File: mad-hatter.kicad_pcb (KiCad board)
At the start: 2 copper layers, 337.2 x 122.6 mm, 161 parts, among them J1 USB_B_Mini, J2 AVR-ISP-6, U1 ATMEGA32U4, X1 16MHz

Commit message: Inverts ISP connector; small fixes
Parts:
- J2: moved to F.Cu
- moved J2 7.85 mm to (304.3, 253.7)
- moved P? 5.39 mm to (305.8, 246.7)
- moved P? 5.39 mm to (310.9, 246.7)
- moved P? 5.39 mm to (308.4, 246.7)
- moved P? 5.39 mm to (303.3, 246.7)
- moved P? 5.39 mm to (298.2, 246.7)
- moved P? 5.39 mm to (300.7, 246.7)
- moved D_PGDN1 4.77 mm to (133.5, 202.7), turned to 180 degrees
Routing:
- net SCK: track 86.4 -> 64.8 mm
- net Net-(D_PGDN1-Pad2): track 5.32 -> 11.3 mm
- net ROW3: track 392.0 -> 387.2 mm
- net +5V: track 164.2 -> 160.0 mm
- net ROW4: track 352.1 -> 354.7 mm
- net MISO: track 55.7 -> 57.7 mm
- net GND: track 107.0 -> 108.0 mm, vias 2 -> 1

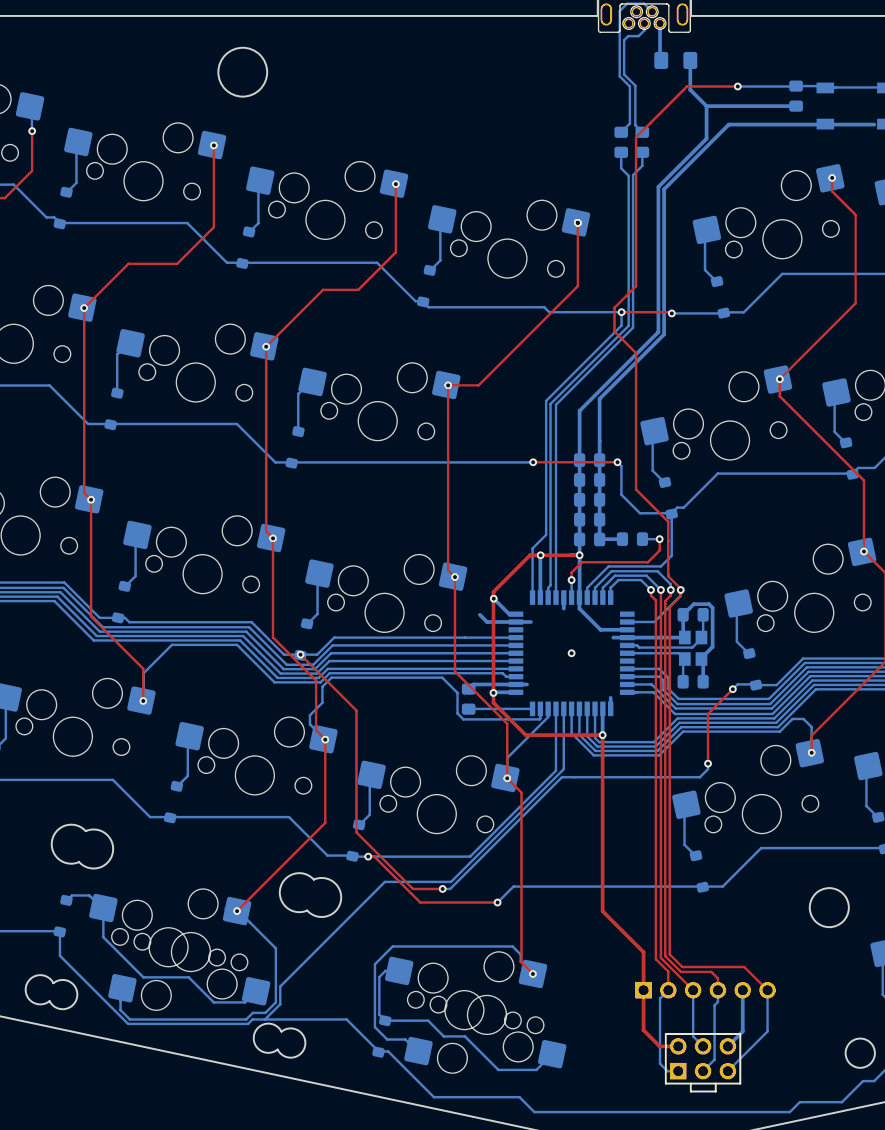
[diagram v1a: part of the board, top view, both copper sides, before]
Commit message: Improves placement of crystal
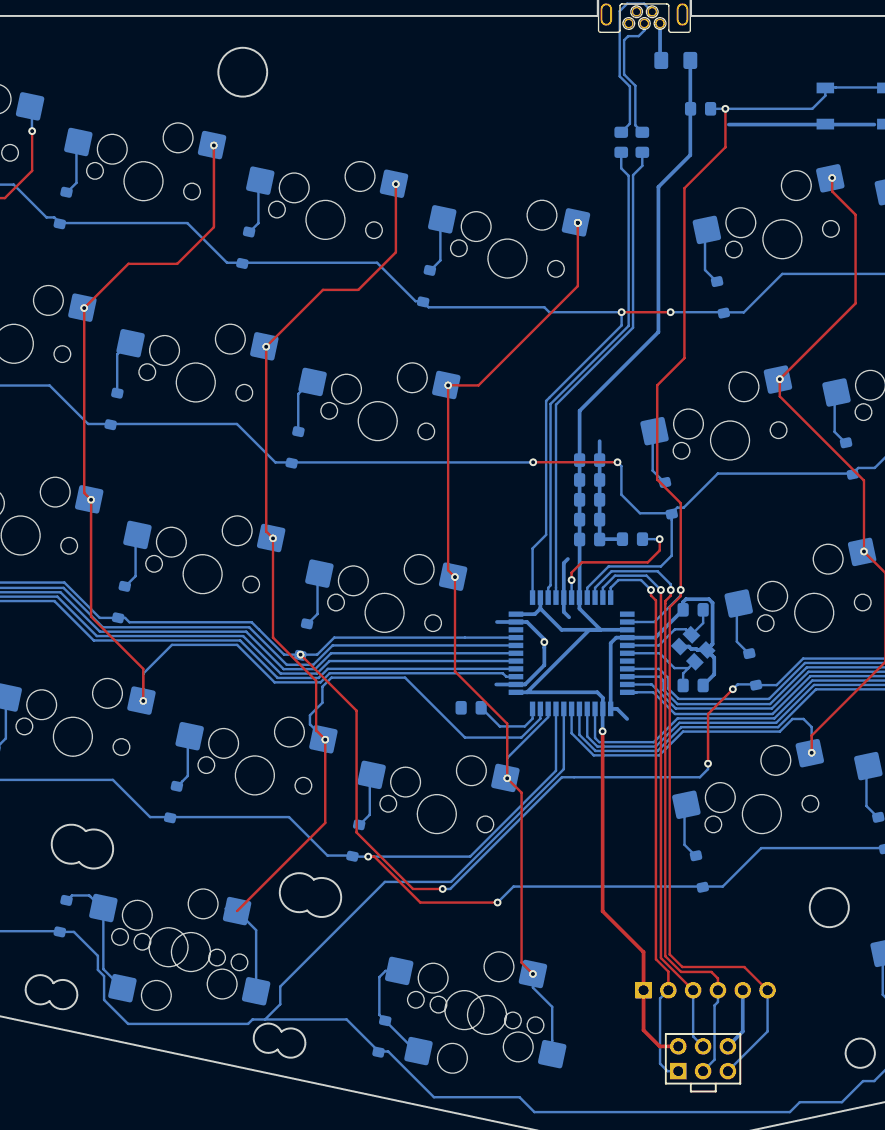
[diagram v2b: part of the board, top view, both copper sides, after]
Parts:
- moved R1 9.87 mm to (304.0, 156.5), turned to 180 degrees
- moved R4 0.92 mm to (280.5, 217.8), turned to 0 degrees
- moved C1 0.51 mm to (303.3, 207.8)
- moved C2 0.38 mm to (303.3, 215.5)
- turned X1 to 315 degrees
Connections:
- J1 pad 6: (no net) -> Net-(J1-Pad6)
- K_GUI1_2 pad 1: COL6 -> Net-(D_GUI1-Pad2)
- K_GUI1_2 pad 2: Net-(D_GUI1-Pad2) -> COL6
- K_SPC1_2 pad 1: COL5 -> Net-(D_SPC1-Pad2)
- K_SPC1_2 pad 2: Net-(D_SPC1-Pad2) -> COL5
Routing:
- net +5V: track 160.0 -> 136.5 mm, vias 5 -> 1
- net COL6: track 127.3 -> 106.1 mm
- net COL5: track 153.3 -> 132.5 mm, vias 5 -> 4
- net GND: track 108.0 -> 88.2 mm
- net Net-(D_GUI1-Pad2): track 26.9 -> 11.7 mm
- net Net-(D_SPC1-Pad2): track 26.2 -> 13.4 mm
- net RST: track 144.4 -> 139.2 mm
- net Net-(C2-Pad1): track 8.54 -> 9.83 mm
- net Net-(R4-Pad2): track 6.55 -> 7.38 mm
- net ROW4: track 354.7 -> 355.5 mm

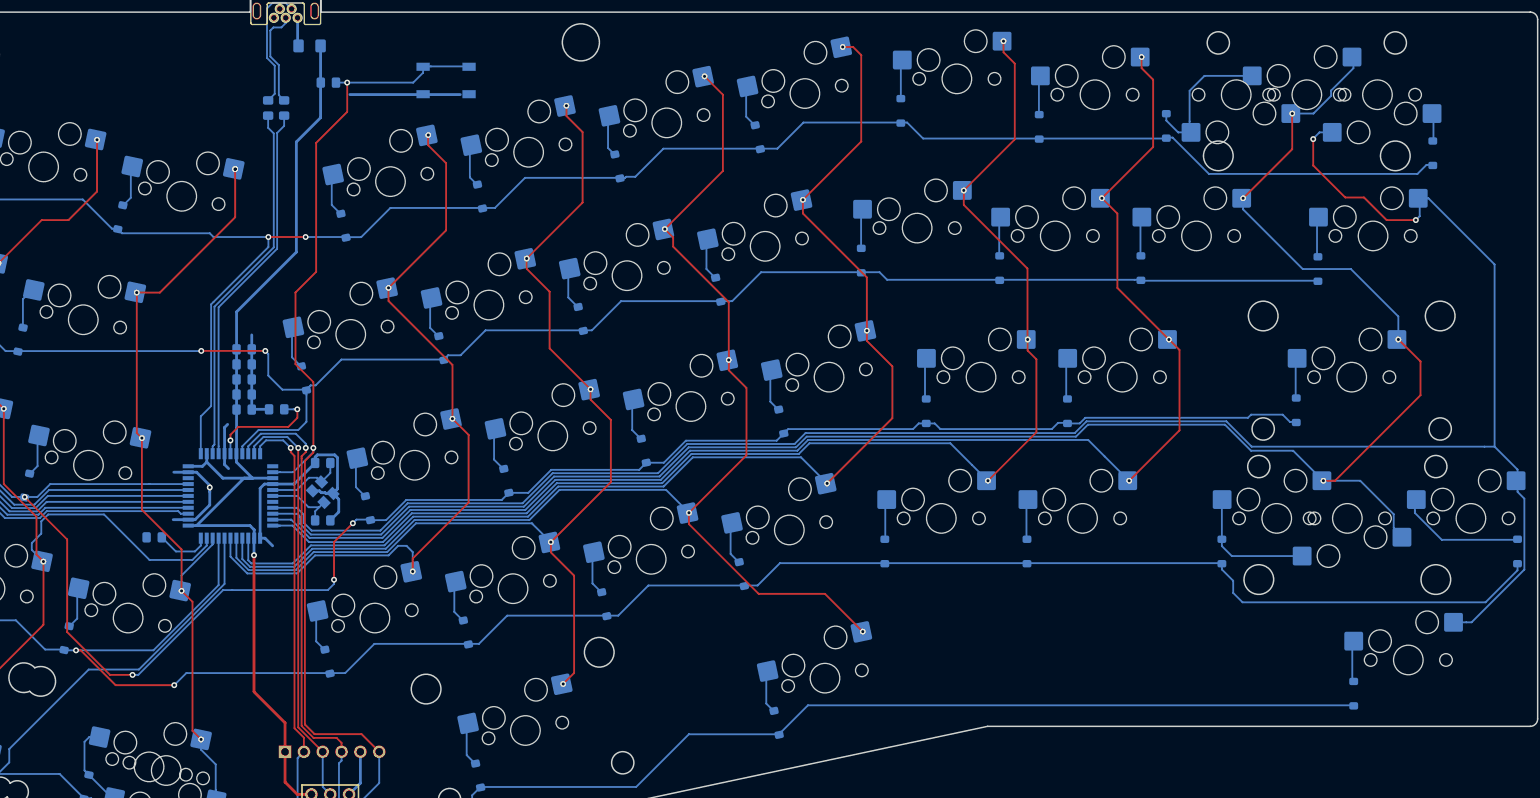
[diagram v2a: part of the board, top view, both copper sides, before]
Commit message: Reorganize capacitors
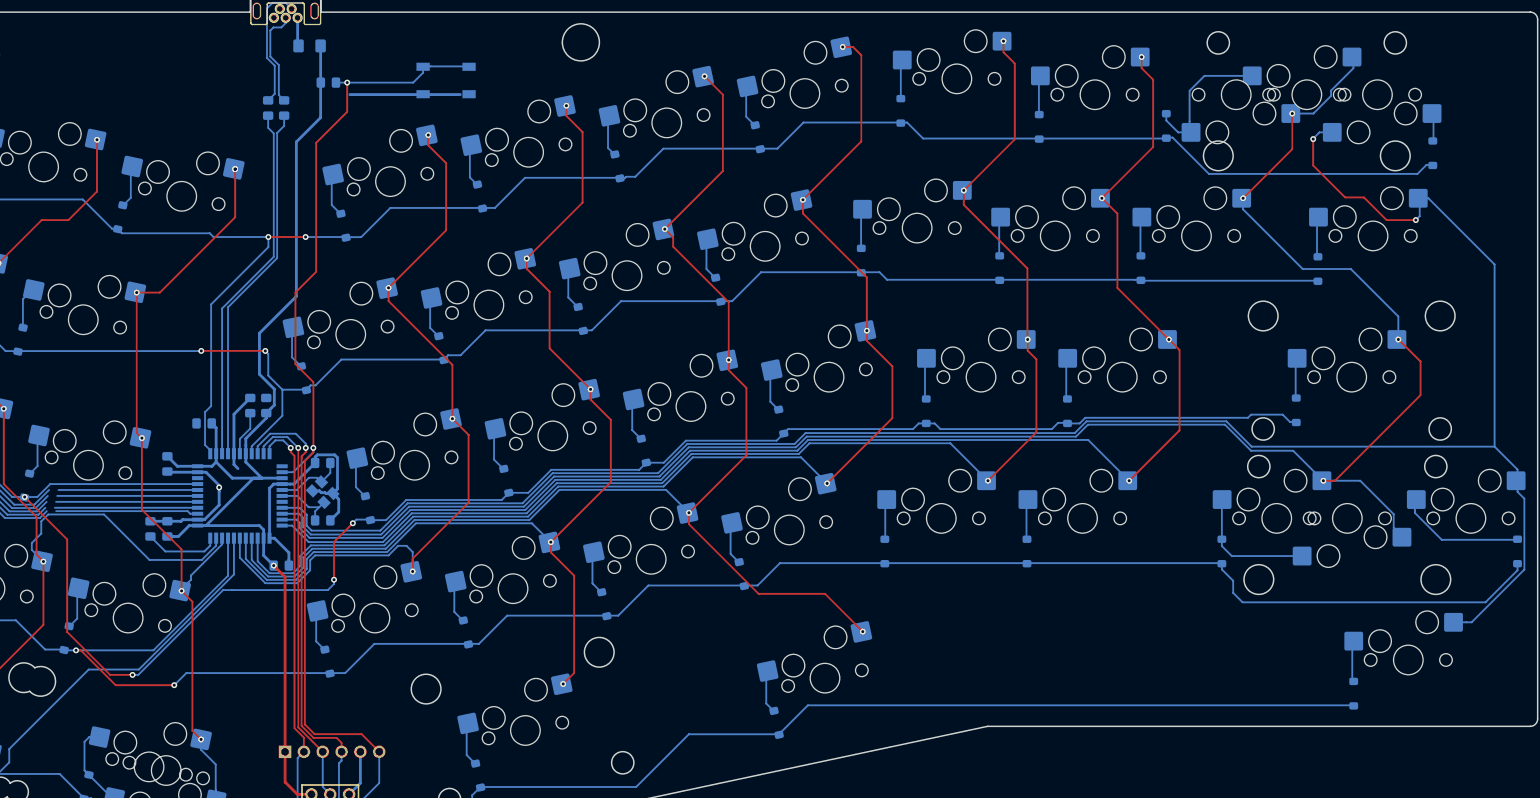
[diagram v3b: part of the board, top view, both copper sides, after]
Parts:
- moved C7 26.3 mm to (282.3, 216.7), turned to 90 degrees
- moved C5 25.6 mm to (297.7, 221.6)
- moved C3 12.7 mm to (282.3, 207.9), turned to 270 degrees
- moved C4 6.66 mm to (287.3, 202.4), turned to 180 degrees
- moved C6 6.30 mm to (295.7, 200.0), turned to 90 degrees
- moved C8 3.60 mm to (293.5, 200.0), turned to 90 degrees
- moved U1 1.27 mm to (292.1, 212.2)
- moved R4 1.25 mm to (280.0, 216.7), turned to 270 degrees
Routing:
- net +5V: track 136.5 -> 151.2 mm
- net Net-(C8-Pad1): track 15.6 -> 6.05 mm, vias 2 -> 0
- net ROW1: track 343.1 -> 338.2 mm
- net Net-(R4-Pad2): track 7.38 -> 10.2 mm
- net COL11: track 175.5 -> 173.3 mm
- net RST: track 139.2 -> 138.0 mm
- net ROW2: track 379.1 -> 380.3 mm
- net Net-(C2-Pad1): track 9.83 -> 8.56 mm
- net Net-(C1-Pad1): track 10.5 -> 9.27 mm
- net MOSI: track 56.6 -> 55.3 mm
- net MISO: track 57.7 -> 56.4 mm
- net SCK: track 64.8 -> 63.5 mm
- net COL5: track 132.5 -> 133.7 mm
- net COL13: track 252.8 -> 251.7 mm
- net COL14: track 269.8 -> 268.7 mm
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
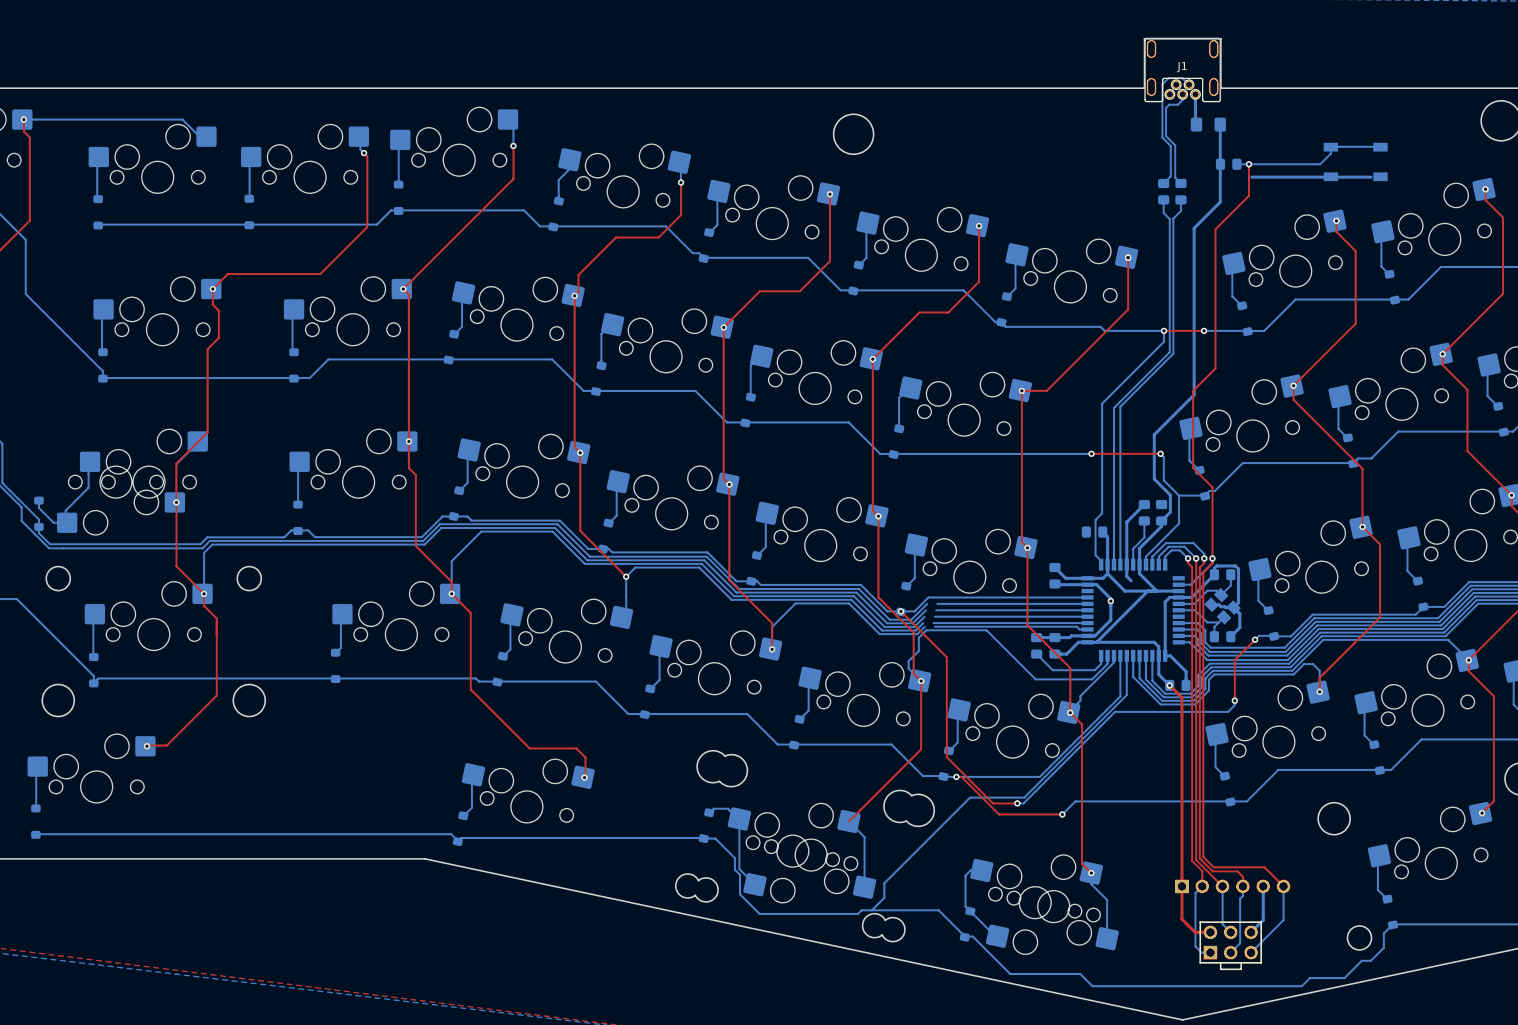
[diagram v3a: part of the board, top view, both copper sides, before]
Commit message: Improves caps placement
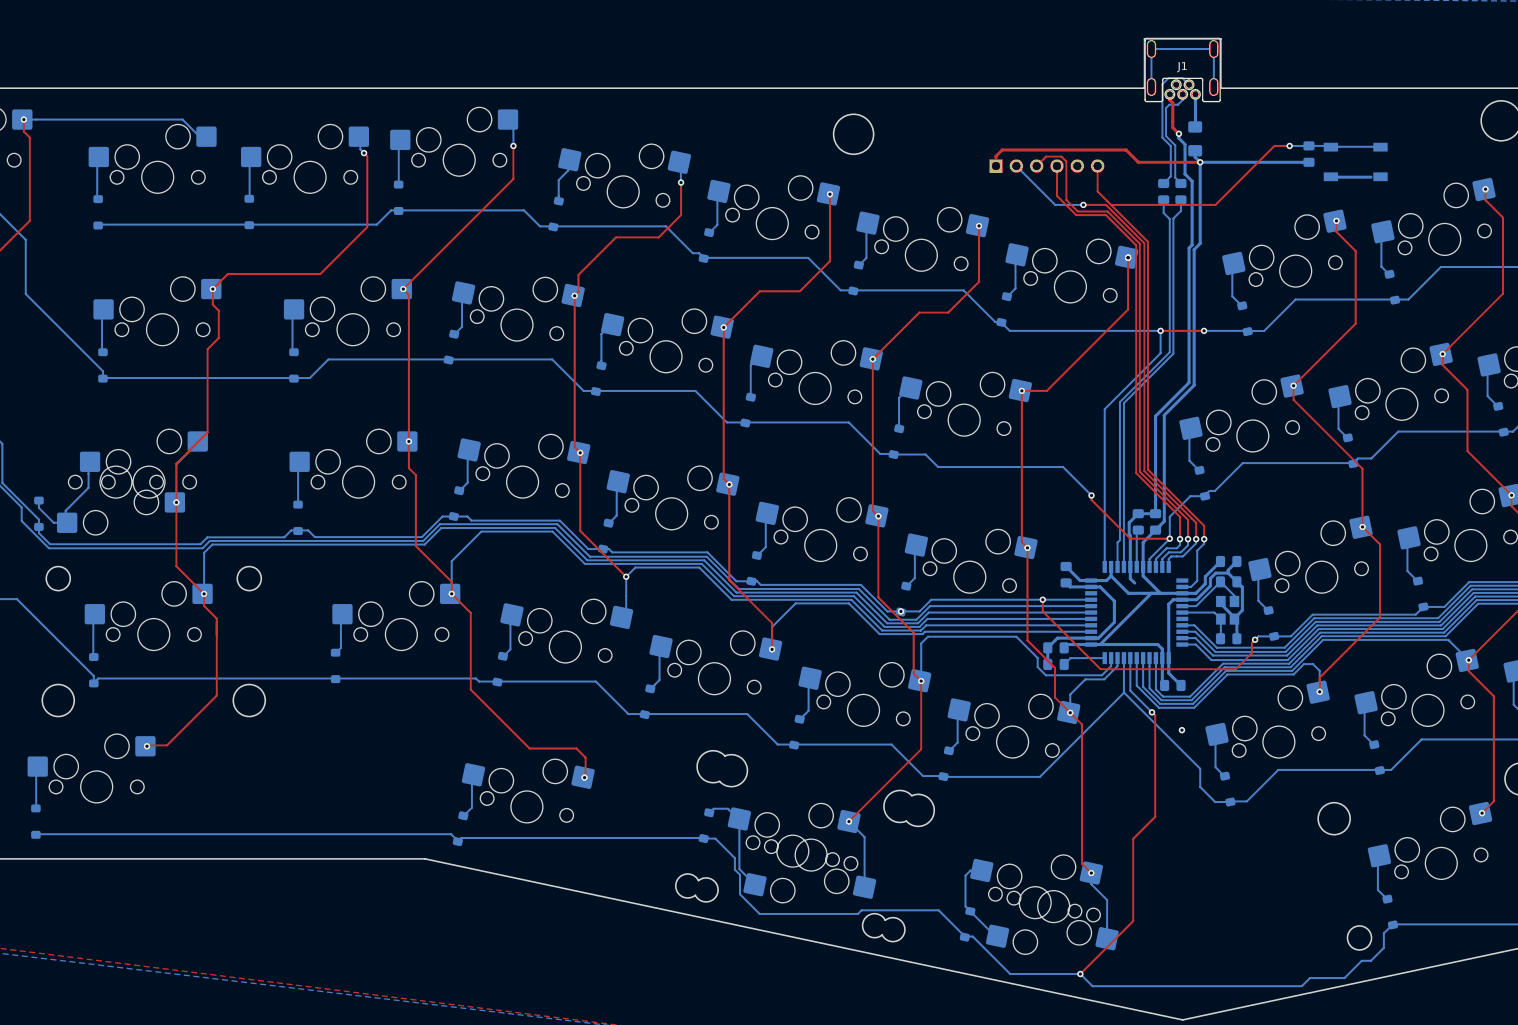
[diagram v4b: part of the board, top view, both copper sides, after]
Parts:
- removed J2: AVR-ISP-6, keyboard_parts:AVR_ICSP_3x2
- moved P? 93.0 mm to (287.7, 156.7)
- moved P? 93.0 mm to (275.0, 156.7)
- moved P? 93.0 mm to (285.1, 156.7)
- moved P? 93.0 mm to (282.6, 156.7)
- moved P? 93.0 mm to (280.0, 156.7)
- moved P? 93.0 mm to (277.5, 156.7)
- moved C3 21.8 mm to (304.0, 206.1), turned to 0 degrees
- moved C4 21.5 mm to (297.1, 221.6), turned to 0 degrees
- moved C7 20.0 mm to (294.9, 201.2)
- moved C5 15.9 mm to (282.4, 216.9), turned to 180 degrees
- moved C6 14.2 mm to (283.7, 207.8), turned to 270 degrees
- moved R1 10.1 mm to (314.1, 155.2), turned to 270 degrees
- moved R4 3.35 mm to (282.4, 219.0), turned to 0 degrees
- moved F1 2.43 mm to (299.8, 153.3), turned to 90 degrees
- moved C8 1.37 mm to (292.7, 201.2)
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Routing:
- net RST: track 138.0 -> 97.0 mm
- net ROW2: track 380.3 -> 340.6 mm, vias 4 -> 3
- net GND: track 88.5 -> 128.1 mm, vias 1 -> 2
- net Net-(J1-Pad6): track 0.00 -> 17.3 mm
- net ROW3: track 387.7 -> 371.1 mm, vias 2 -> 0
- net MOSI: track 55.3 -> 65.8 mm
- net MISO: track 56.4 -> 65.4 mm, vias 1 -> 2
- net Net-(R4-Pad2): track 10.2 -> 5.40 mm
- net ROW4: track 356.0 -> 351.7 mm, vias 0 -> 2
- net SCK: track 63.5 -> 60.7 mm
- net COL5: track 133.7 -> 131.8 mm, vias 4 -> 5
- net COL1: track 232.7 -> 234.3 mm
- net COL0: track 224.1 -> 225.7 mm
- net COL2: track 190.7 -> 192.3 mm
- net COL3: track 128.9 -> 130.5 mm
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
